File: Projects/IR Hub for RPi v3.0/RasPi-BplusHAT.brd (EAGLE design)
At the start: 65 x 56 mm, 39 parts, among them SW1 SPST_TACT-KMR2, SW2 SPST_TACT-KMR2, SW3 SPST_TACT-KMR2, T1 2N4401, T2 2N4401, T3 2N4401, T4 2N4401

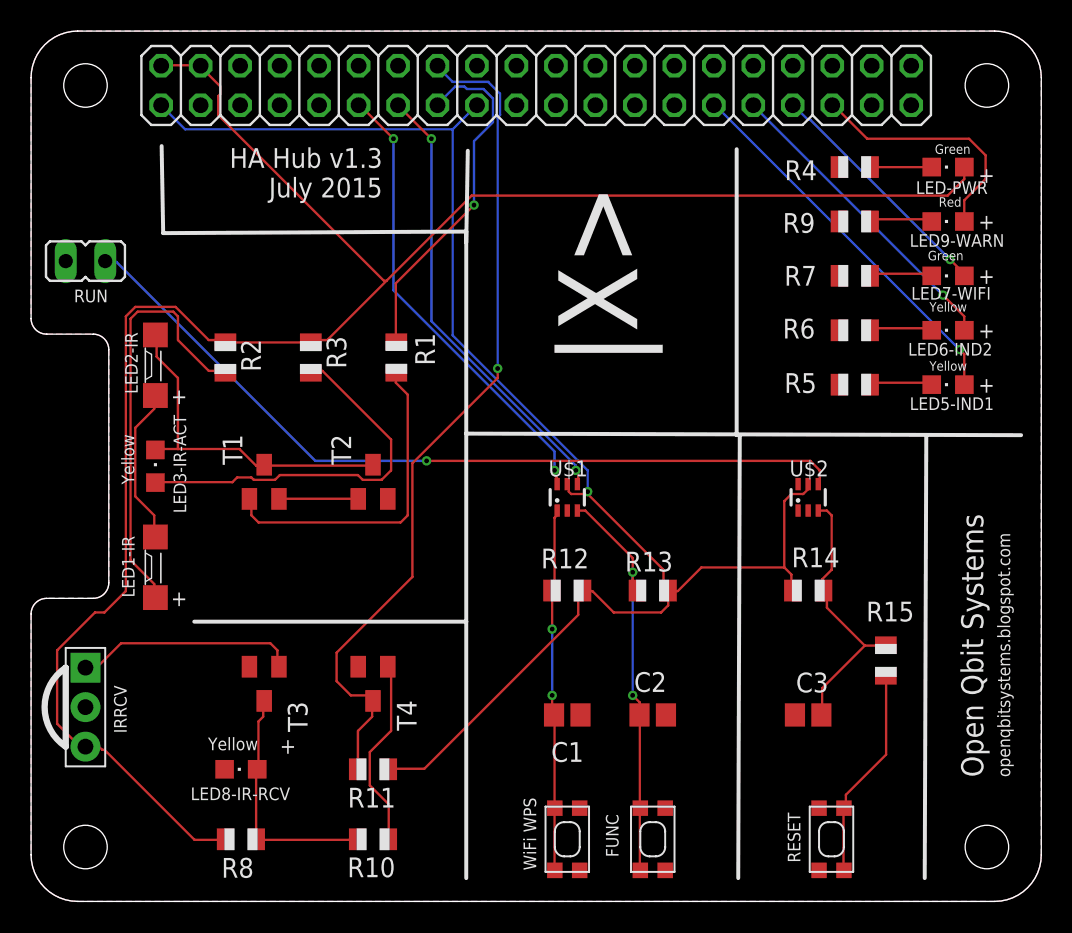
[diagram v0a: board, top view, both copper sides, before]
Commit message: Revert "relocated IRRCV"
This reverts commit a5258da49ac38eba7fe15d274991cfdce8bd6922.
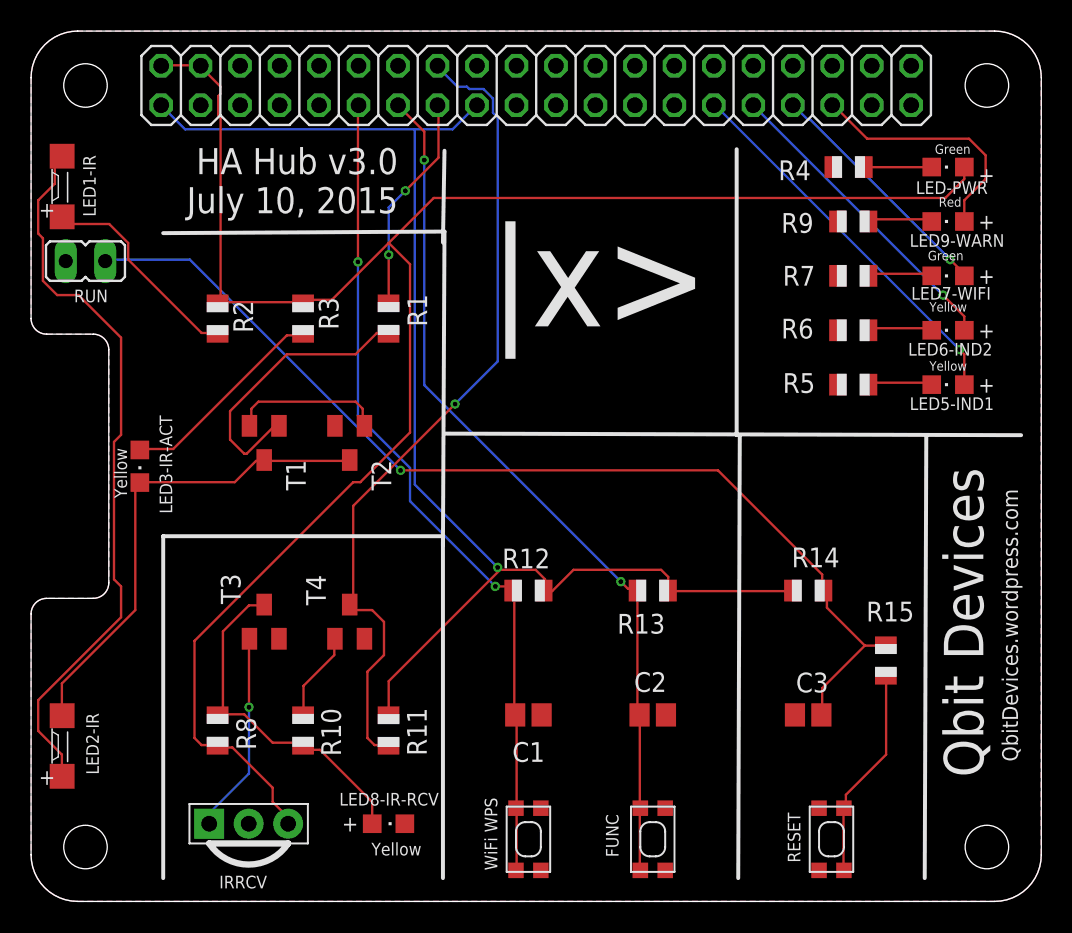
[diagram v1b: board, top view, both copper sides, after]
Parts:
- removed U$1, U$2: 74HC2G17-Q100, varshneya:SC-70-6L
- RUN: value RST -> (none)
- moved LED1-IR 25.2 mm to (2.00, 46.0)
- moved LED2-IR 25.2 mm to (2.00, 10.0)
- moved IRRCV 12.9 mm to (14.0, 5.00), turned to 0 degrees
- moved LED8-IR-RCV 10.1 mm to (23.0, 5.00), turned to 270 degrees
- moved R10 8.32 mm to (17.5, 11.0), turned to 270 degrees
- moved R8 7.16 mm to (12.0, 11.0), turned to 270 degrees
- moved T4 4.27 mm to (20.5, 18.0), turned to 0 degrees
- moved T3 4.00 mm to (15.0, 18.0), turned to 0 degrees
- moved T2 2.92 mm to (20.5, 29.5), turned to 180 degrees
- moved R11 2.69 mm to (23.0, 11.0), turned to 90 degrees
- moved R1 2.55 mm to (23.0, 37.5)
- moved R2 2.55 mm to (12.0, 37.5)
- moved R3 2.55 mm to (17.5, 37.5)
- moved C1 2.50 mm to (32.0, 12.0)
- moved R12 2.50 mm to (32.0, 20.0)
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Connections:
- removed net N$12: C2.1, R13.1, SW2.1, SW2.3, U$1.3
- removed net N$13: C3.1, R14.1, R15.1, U$2.3
- removed net N$9: C1.1, R12.1, SW1.2, SW1.4, U$1.1
- net +3V3: no longer U$1.5, U$2.5
- net GND: no longer U$1.2, U$2.2
- net GPIO17: now also C1.1, R12.1, SW1.2, SW1.4; no longer U$1.6
- net GPIO27: now also C2.1, R13.1, SW2.1, SW2.3; no longer U$1.4
- net RST: now also C3.1, R14.1, R15.1; no longer U$2.4
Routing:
- net N$3: track 10.2 -> 46.8 mm
- net GPIO27: track 29.2 -> 56.0 mm
- net N$12: track 26.4 -> 0.00 mm, vias 2 -> 0
- net GPIO17: track 29.7 -> 54.1 mm
- net N$9: track 23.4 -> 0.00 mm, vias 2 -> 0
- net N$13: track 17.7 -> 0.00 mm
- net RST: track 52.5 -> 67.3 mm
- net +3V3: track 100.4 -> 86.1 mm
- net N$2: track 27.5 -> 13.7 mm
- net N$6: track 24.9 -> 13.6 mm
- net N$4: track 22.5 -> 31.2 mm
- net GPIO22: track 22.7 -> 14.1 mm, vias 1 -> 2
- net N$10: track 15.6 -> 22.8 mm
- net N$23: track 12.3 -> 5.73 mm
- net +5V: track 124.3 -> 118.3 mm
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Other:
- board text added: "HA Hub v3.0 July 10, 2015"
- board text added: "Home Automation Hub v3.0"
- board text added: "Qbit Devices"
- board text added: "QbitDevices.wordpress.com"
- board text added: "TODO 1. Add schmitt buffers for all the push buttons 2. check the polarity of the IR LEDs 3. Check both ICs wrt 74HC/74LV/... for 3.3V DONE 1. ELIMINATED - Verify the Watchdog circuit 2. ELIMINATED - Will RPi gpio go in a state to allow disabling WD? 3. Ensure long push for RESET push button (cap and resistor values) 4. Move Power LED to the Status LEDs area 5. check RUN location 6. Verify the IR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"
- board text added: "|x>"
- board text removed: "HA Hub v1.3 July 2015"
- board text removed: "Home Automation Hub v1.3"
- board text removed: "Open Qbit Systems"
- board text removed: "TODO 1. Check the Schmitt debouncing on breadboard 2. check the polarity of the IR LEDs 3. Check both ICs wrt 74HC/74LV/... for 3.3V DONE 1. Add schmitt buffers for all the push buttons (create part) 2. ELIMINATED - Verify the Watchdog circuit 3. ELIMINATED - Will RPi gpio go in a state to allow disabling WD? 4. Ensure long push for RESET push button (cap and resistor values) 5. Move Power LED to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"
- board text removed: "openqbitsystems.blogspot.com"
- board text removed: "|X>"
